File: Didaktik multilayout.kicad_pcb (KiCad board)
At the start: 2 copper layers, 212.7 x 79.4 mm, 121 parts, among them J1 Conn_01x04_MountingPin, J2 AVR-ISP-6, SW1 SW_Push_45deg, SW10 SW_Push_45deg, SW11 SW_Push_45deg, SW12 SW_Push_45deg, SW13 SW_Push_45deg, SW14 SW_Push_45deg, SW15 SW_Push_45deg, SW16 SW_Push_45deg, SW17 SW_Push_45deg, SW18 SW_Push_45deg, SW19 SW_Push_45deg, SW2 SW_Push_45deg, SW20 SW_Push_45deg, SW21 SW_Push_45deg, SW22 SW_Push_45deg, SW23 SW_Push_45deg, SW24 SW_Push_45deg, SW25 SW_Push_45deg, SW26 SW_Push_45deg, SW27 SW_Push_45deg, SW28 SW_Push_45deg, SW29 SW_Push_45deg, SW3 SW_Push_45deg, SW30 SW_Push_45deg, SW31 SW_Push_45deg, SW31a1 SW_Push_45deg, SW32 SW_Push_45deg, SW32a1 SW_Push_45deg, SW33 SW_Push_45deg, SW33a1 SW_Push_45deg, SW34 SW_Push_45deg, SW34a1 SW_Push_45deg, SW34b1 SW_Push_45deg, SW35 SW_Push_45deg, SW35a1 SW_Push_45deg, SW35b1 SW_Push_45deg, SW35c1 SW_Push_45deg, SW36 SW_Push_45deg, SW36a1 SW_Push_45deg, SW36b1 SW_Push_45deg, SW36c1 SW_Push_45deg, SW37 SW_Push_45deg, SW37a1 SW_Push_45deg, SW37b1 SW_Push_45deg, SW38 SW_Push_45deg, SW38a1 SW_Push_45deg, SW39 SW_Push_45deg, SW39a1 SW_Push_45deg, SW4 SW_Push_45deg, SW40 SW_Push_45deg, SW40a1 SW_Push_45deg, SW5 SW_Push_45deg, SW6 SW_Push_45deg, SW7 SW_Push_45deg, SW8 SW_Push_45deg, SW9 SW_Push_45deg, U1 ATmega32U4-M, Y1 Crystal_GND24_Small

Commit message: routing multipcb
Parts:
- moved D33 19.0 mm to (203.2, 106.4)
- moved D37 11.1 mm to (214.3, 104.8)
- moved D20 9.53 mm to (136.5, 104.8)
- moved D29 9.53 mm to (174.6, 104.8)
- moved D12 9.52 mm to (98.4, 104.8)
- moved D24 9.52 mm to (155.6, 106.4)
- moved D16 6.35 mm to (114.3, 106.4)
- moved D32 6.35 mm to (200.0, 87.3)
- moved D41 4.76 mm to (231.8, 106.4)
- moved D7 4.76 mm to (84.1, 87.3)
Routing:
- net COL2: track 307.6 -> 372.0 mm
- net +5V: track 323.7 -> 284.8 mm
- net MISO: track 37.2 -> 0.00 mm, vias 2 -> 0
- net MOSI: track 34.8 -> 0.00 mm, vias 2 -> 0
- net SCK: track 31.5 -> 0.00 mm, vias 2 -> 0
- net ROW4: track 374.4 -> 403.8 mm
- net ROW5: track 351.7 -> 379.5 mm
- net Net-(D33-Pad2): track 18.3 -> 45.4 mm
- net COL4: track 395.4 -> 419.1 mm
- net Net-(D12-Pad2): track 14.7 -> 37.9 mm, vias 0 -> 2
- net Net-(D8-Pad2): track 18.5 -> 40.9 mm
- net COL3: track 354.0 -> 375.3 mm
- net Net-(D24-Pad2): track 18.3 -> 38.3 mm
- net Net-(D20-Pad2): track 14.7 -> 34.2 mm, vias 0 -> 2
- net Net-(SW34b1-Pad2): track 18.3 -> 34.6 mm
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
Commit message: set up multilayout
need to check if all switches are really routed
maybe get rid of 2U
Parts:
- moved J2 168.8 mm to (69.8, 81.2)
- moved G*** 0.76 mm to (136.5, 85.0)
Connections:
- D12 pad 2: Net-(D12-Pad2) -> COL0
- D16 pad 2: Net-(SW34b1-Pad2) -> COL1
- D20 pad 2: Net-(D20-Pad2) -> COL1
- D24 pad 2: Net-(D24-Pad2) -> COL1
- D33 pad 2: Net-(D33-Pad2) -> COL3
- D37 pad 2: Net-(D37-Pad2) -> COL4
- D41 pad 2: Net-(D41-Pad2) -> COL4
- SW15 pad 1: COL2 -> COL1
- SW16 pad 1: COL2 -> COL1
- SW25 pad 1: COL2 -> COL1
- SW26 pad 1: COL2 -> COL1
- SW34 pad 2: Net-(SW34b1-Pad2) -> COL1
- SW34a1 pad 2: Net-(SW34b1-Pad2) -> COL1
- SW34b1 pad 2: Net-(SW34b1-Pad2) -> COL1
- SW35 pad : (no net) -> COL1
- SW35 pad 1: COL2 -> COL1
- SW35 pad 2: Net-(D20-Pad2) -> COL1
- SW35a1 pad : (no net) -> COL1
- SW35a1 pad 1: COL2 -> COL1
- SW35a1 pad 2: Net-(D20-Pad2) -> COL1
- SW35b1 pad : (no net) -> COL1
- SW35b1 pad 1: COL2 -> COL1
- SW35b1 pad 2: Net-(D20-Pad2) -> COL1
- SW35c1 pad 1: COL2 -> COL1
- SW35c1 pad 2: Net-(D20-Pad2) -> COL1
- SW36 pad : (no net) -> COL1
- SW36 pad 1: COL2 -> COL1
- SW36 pad 2: Net-(D24-Pad2) -> COL1
- SW36a1 pad : (no net) -> COL1
- SW36a1 pad 1: COL2 -> COL1
- SW36a1 pad 2: Net-(D24-Pad2) -> COL1
- SW36b1 pad : (no net) -> COL1
- SW36b1 pad 1: COL2 -> COL1
- SW36b1 pad 2: Net-(D24-Pad2) -> COL1
- SW36c1 pad 1: COL2 -> COL1
- SW36c1 pad 2: Net-(D20-Pad2) -> COL1
- SW37b1 pad : (no net) -> COL1
- SW5 pad 1: COL2 -> COL1
- SW6 pad 1: COL2 -> COL1
- U1 pad 20: unconnected-(U1-Pad20) -> SCK
- U1 pad 21: ROW5 -> MISO
- U1 pad 22: ROW4 -> MOSI
- U1 pad 26: MOSI -> unconnected-(U1-Pad26)
- U1 pad 27: SCK -> ROW7
- U1 pad 28: MISO -> ROW6
- U1 pad 29: ROW7 -> ROW5
- U1 pad 30: ROW6 -> ROW4
- U1 pad 37: COL2 -> COL1
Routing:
- net COL1: track 279.3 -> 793.9 mm, vias 1 -> 8
- net COL2: track 372.0 -> 0.00 mm, vias 1 -> 0
- net COL3: track 375.3 -> 453.7 mm, vias 1 -> 3
- net COL4: track 419.1 -> 494.2 mm, vias 1 -> 5
- net Net-(D33-Pad2): track 45.4 -> 0.00 mm, vias 2 -> 0
- net MOSI: track 0.00 -> 39.2 mm, vias 0 -> 2
- net Net-(D24-Pad2): track 38.3 -> 0.00 mm, vias 2 -> 0
- net SCK: track 0.00 -> 38.2 mm, vias 0 -> 2
- net Net-(D12-Pad2): track 37.9 -> 0.00 mm, vias 2 -> 0
- net COL0: track 246.2 -> 282.5 mm, vias 1 -> 3
- net Net-(SW34b1-Pad2): track 34.6 -> 0.00 mm, vias 2 -> 0
- net Net-(D20-Pad2): track 34.2 -> 0.00 mm, vias 2 -> 0
- net MISO: track 0.00 -> 34.1 mm, vias 0 -> 2
- net +5V: track 284.8 -> 318.9 mm, vias 5 -> 7
- net Net-(D41-Pad2): track 31.6 -> 0.00 mm, vias 2 -> 0
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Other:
- board text added: "1.5U"
- board text added: "2U"
- board text added: "3U"
- board text added: "6U"
- board text added: "7U"
- board text added: "check rewiring and pcb border"
- board text removed: "reset set up"
- board text removed: "rewiring everything"

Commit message: changes
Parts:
- added SW1: SW_Push_45deg, Keebio-Parts:MX-Alps-Choc-1U-NoLED, F.Cu at (21.6, 40.3)
- added SW10: SW_Push_45deg, Keebio-Parts:MX-Alps-Choc-1U-NoLED, F.Cu at (103.9, 169.7)
- added SW11: SW_Push_45deg, Keebio-Parts:MX-Alps-Choc-1U-NoLED, F.Cu at (114.6, 210.1)
- added SW12: SW_Push_45deg, Keebio-Parts:MX-Alps-Choc-1U-NoLED, F.Cu at (144.3, 169.7)
- added SW13: SW_Push_45deg, Keebio-Parts:MX-Alps-Choc-1U-NoLED, F.Cu at (74.2, 230.3)
- added SW14: SW_Push_45deg, Keebio-Parts:MX-Alps-Choc-1U-NoLED, F.Cu at (103.9, 149.5)
- added SW15: SW_Push_45deg, Keebio-Parts:MX-Alps-Choc-1U-NoLED, F.Cu at (175.2, 230.3)
- added SW16: SW_Push_45deg, Keebio-Parts:MX-Alps-Choc-1U-NoLED, F.Cu at (164.5, 169.7)
- added SW17: SW_Push_45deg, Keebio-Parts:MX-Alps-Choc-1U-NoLED, F.Cu at (114.6, 189.9)
- added SW18: SW_Push_45deg, Keebio-Parts:MX-Alps-Choc-1U-NoLED, F.Cu at (175.2, 189.9)
- added SW19: SW_Push_45deg, Keebio-Parts:MX-Alps-Choc-1U-NoLED, F.Cu at (124.1, 149.5)
- added SW2: SW_Push_45deg, Keebio-Parts:MX-Alps-Choc-1U-NoLED, F.Cu at (164.5, 149.5)
- added SW20: SW_Push_45deg, Keebio-Parts:MX-Alps-Choc-1U-NoLED, F.Cu at (175.2, 210.1)
- added SW21: SW_Push_45deg, Keebio-Parts:MX-Alps-Choc-1U-NoLED, F.Cu at (225.1, 149.5)
- added SW22: SW_Push_45deg, Keebio-Parts:MX-Alps-Choc-1U-NoLED, F.Cu at (134.8, 230.3)
- added SW23: SW_Push_45deg, Keebio-Parts:MX-Alps-Choc-1U-NoLED, F.Cu at (83.7, 169.7)
- added SW24: SW_Push_45deg, Keebio-Parts:MX-Alps-Choc-1U-NoLED, F.Cu at (184.7, 149.5)
- added SW25: SW_Push_45deg, Keebio-Parts:MX-Alps-Choc-1U-NoLED, F.Cu at (204.9, 149.5)
- added SW26: SW_Push_45deg, Keebio-Parts:MX-Alps-Choc-1U-NoLED, F.Cu at (134.8, 210.1)
- added SW27: SW_Push_45deg, Keebio-Parts:MX-Alps-Choc-1U-NoLED, F.Cu at (195.4, 189.9)
- added SW28: SW_Push_45deg, Keebio-Parts:MX-Alps-Choc-1U-NoLED, F.Cu at (74.2, 210.1)
- added SW29: SW_Push_45deg, Keebio-Parts:MX-Alps-Choc-1U-NoLED, F.Cu at (83.7, 149.5)
- added SW3: SW_Push_45deg, Keebio-Parts:MX-Alps-Choc-1U-NoLED, F.Cu at (94.4, 189.9)
- added SW30: SW_Push_45deg, Keebio-Parts:MX-Alps-Choc-1U-NoLED, F.Cu at (94.4, 230.3)
- added SW31: SW_Push_45deg, Keebio-Parts:MX-Alps-Choc-1.5U-NoLED, F.Cu at (58.7, 169.7)
- added SW32: SW_Push_45deg, Keebio-Parts:MX-Alps-Choc-1U-NoLED, F.Cu at (155.0, 189.9)
- added SW33: SW_Push_45deg, Keebio-Parts:MX-Alps-Choc-1U-NoLED, F.Cu at (54.0, 210.1)
- added SW34: SW_Push_45deg, Keebio-Parts:MX-Alps-Choc-1U-NoLED, F.Cu at (155.0, 230.3)
- added SW35: SW_Push_45deg, Keebio-Parts:MX-Alps-Choc-1U-NoLED, F.Cu at (26.7, 175.6)
- added SW36: SW_Push_45deg, Keebio-Parts:MX-Alps-Choc-1U-NoLED, F.Cu at (114.6, 230.3)
- added SW37: SW_Push_45deg, Keebio-Parts:MX-Alps-Choc-1U-NoLED, F.Cu at (74.2, 189.9)
- added SW38: SW_Push_45deg, Keebio-Parts:MX-Alps-Choc-1U-NoLED, F.Cu at (144.3, 149.5)
- added SW39: SW_Push_45deg, Keebio-Parts:MX-Alps-Choc-1U-NoLED, F.Cu at (155.0, 210.1)
- added SW4: SW_Push_45deg, Keebio-Parts:MX-Alps-Choc-1U-NoLED, F.Cu at (184.7, 169.7)
- added SW40: SW_Push_45deg, Keebio-Parts:MX-Alps-Choc-1.5U-NoLED, F.Cu at (58.7, 149.5)
- added SW5: SW_Push_45deg, Keebio-Parts:MX-Alps-Choc-1U-NoLED, F.Cu at (134.8, 189.9)
- added SW6: SW_Push_45deg, Keebio-Parts:MX-Alps-Choc-1U-NoLED, F.Cu at (94.4, 210.1)
- added SW7: SW_Push_45deg, Keebio-Parts:MX-Alps-Choc-1U-NoLED, F.Cu at (204.9, 169.7)
- added SW8: SW_Push_45deg, Keebio-Parts:MX-Alps-Choc-1U-NoLED, F.Cu at (225.1, 169.7)
- added SW9: SW_Push_45deg, Keebio-Parts:MX-Alps-Choc-1U-NoLED, F.Cu at (124.1, 169.7)
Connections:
- D12 pad 2: COL0 -> Net-(D12-Pad2)
- D16 pad 2: COL1 -> Net-(D16-Pad2)
- D20 pad 2: COL1 -> Net-(D20-Pad2)
- D24 pad 2: COL1 -> Net-(D24-Pad2)
- D33 pad 2: COL3 -> Net-(D33-Pad2)
- D37 pad 2: COL4 -> Net-(D37-Pad2)
- D41 pad 2: COL4 -> Net-(D41-Pad2)
- SW34a1 pad 2: COL1 -> Net-(D16-Pad2)
- SW34b1 pad 2: COL1 -> Net-(D16-Pad2)
- SW35a1 pad : COL1 -> (no net)
- SW35a1 pad 1: COL1 -> COL2
- SW35a1 pad 2: COL1 -> Net-(D20-Pad2)
- SW35b1 pad : COL1 -> (no net)
- SW35b1 pad 1: COL1 -> COL2
- SW35b1 pad 2: COL1 -> Net-(D20-Pad2)
- SW35c1 pad 1: COL1 -> COL2
- SW35c1 pad 2: COL1 -> Net-(D20-Pad2)
- SW36a1 pad : COL1 -> (no net)
- SW36a1 pad 1: COL1 -> COL2
- SW36a1 pad 2: COL1 -> Net-(D24-Pad2)
- SW36b1 pad : COL1 -> (no net)
- SW36b1 pad 1: COL1 -> COL2
- SW36b1 pad 2: COL1 -> Net-(D24-Pad2)
- SW36c1 pad 1: COL1 -> COL2
- SW36c1 pad 2: COL1 -> Net-(D20-Pad2)
- SW37b1 pad : COL1 -> (no net)
- U1 pad 37: COL1 -> COL2
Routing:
- net GND: track 53.5 -> 61.6 mm, vias 17 -> 18
- net (no net): vias 0 -> 1
- added copper zone on B.Cu, net (none)
- added copper zone on F.Cu, net (none)
- removed copper zone on B.Cu, net GND
- removed copper zone on F.Cu, net GND

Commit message: cleaning up the schematics / pcb for multi
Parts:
- removed the SW1 at (41.3, 41.3)
- removed the SW10 at (103.9, 169.7)
- removed the SW11 at (114.6, 210.1)
- removed the SW12 at (144.3, 169.7)
- removed the SW13 at (74.2, 230.3)
- removed the SW14 at (108.0, 60.3)
- removed the SW15 at (127.0, 60.3)
- removed the SW16 at (164.5, 169.7)
- removed the SW17 at (114.6, 189.9)
- removed the SW18 at (175.2, 189.9)
- removed the SW19 at (124.1, 149.5)
- removed the SW2 at (60.3, 41.3)
- removed the SW20 at (222.2, 60.3)
- removed the SW21 at (60.3, 79.4)
- removed the SW22 at (79.4, 79.4)
- removed the SW23 at (83.7, 169.7)
- removed the SW24 at (117.5, 79.4)
- removed the SW25 at (204.9, 149.5)
- removed the SW26 at (134.8, 210.1)
- removed the SW27 at (174.6, 79.4)
- removed the SW28 at (74.2, 210.1)
- removed the SW29 at (212.7, 79.4)
- removed the SW3 at (94.4, 189.9)
- removed the SW30 at (94.4, 230.3)
- removed the SW31 at (58.7, 169.7)
- removed the SW32 at (155.0, 189.9)
- removed the SW33 at (54.0, 210.1)
- removed the SW34 at (155.0, 230.3)
- removed the SW35 at (26.7, 175.6)
- removed the SW36 at (114.6, 230.3)
- removed the SW37 at (74.2, 189.9)
- removed the SW38 at (144.3, 149.5)
- removed the SW39 at (155.0, 210.1)
- removed the SW4 at (184.7, 169.7)
- removed the SW40 at (58.7, 149.5)
- removed the SW5 at (117.5, 41.3)
- removed the SW6 at (136.5, 41.3)
- removed the SW7 at (155.6, 41.3)
- removed the SW8 at (174.6, 41.3)
- removed the SW9 at (124.1, 169.7)
- moved SW21 179.1 mm to (60.3, 79.4)
- moved SW15 176.6 mm to (127.0, 60.3)
- moved SW6 173.9 mm to (136.4, 41.3)
- moved SW22 160.7 mm to (79.4, 79.4)
- moved SW20 157.0 mm to (222.2, 60.3)
- moved SW2 150.2 mm to (60.3, 41.3)
- moved SW5 149.6 mm to (117.5, 41.3)
- moved SW29 146.8 mm to (212.7, 79.4)
- moved SW8 138.0 mm to (174.6, 41.3)
- moved SW7 137.5 mm to (155.6, 41.3)
- moved SW27 112.4 mm to (174.6, 79.4)
- moved SW24 97.1 mm to (117.5, 79.4)
- moved SW14 89.2 mm to (108.0, 60.3)
- moved SW1 19.7 mm to (41.3, 41.3)
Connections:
- SW16 pad 1: COL1 -> COL2
- SW25 pad 1: COL1 -> COL2
- SW26 pad 1: COL1 -> COL2
- SW33 pad 1: COL1 -> (no net)
- SW33 pad 2: Net-(D12-Pad2) -> (no net)
- SW34 pad 2: COL1 -> Net-(D16-Pad2)
- SW35 pad : COL1 -> (no net)
- SW35 pad 1: COL1 -> COL2
- SW35 pad 2: COL1 -> Net-(D20-Pad2)
- SW36 pad : COL1 -> (no net)
- SW36 pad 1: COL1 -> COL2
- SW36 pad 2: COL1 -> Net-(D24-Pad2)
- SW9 pad 1: COL4 -> (no net)
- SW9 pad 2: Net-(D34-Pad2) -> (no net)
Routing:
- net COL2: track 0.00 -> 793.9 mm, vias 0 -> 8
- net COL1: track 793.9 -> 0.00 mm, vias 8 -> 0
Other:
- board text removed: "Didaktik 40"

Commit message: work on multi
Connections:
- SW33 pad 1: (no net) -> COL1
- SW33 pad 2: (no net) -> Net-(D12-Pad2)
- SW9 pad 1: (no net) -> COL4
- SW9 pad 2: (no net) -> Net-(D34-Pad2)
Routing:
- net (no net): track 0.00 -> 8.54 mm, vias 1 -> 3
- net GND: track 61.6 -> 53.4 mm, vias 18 -> 16

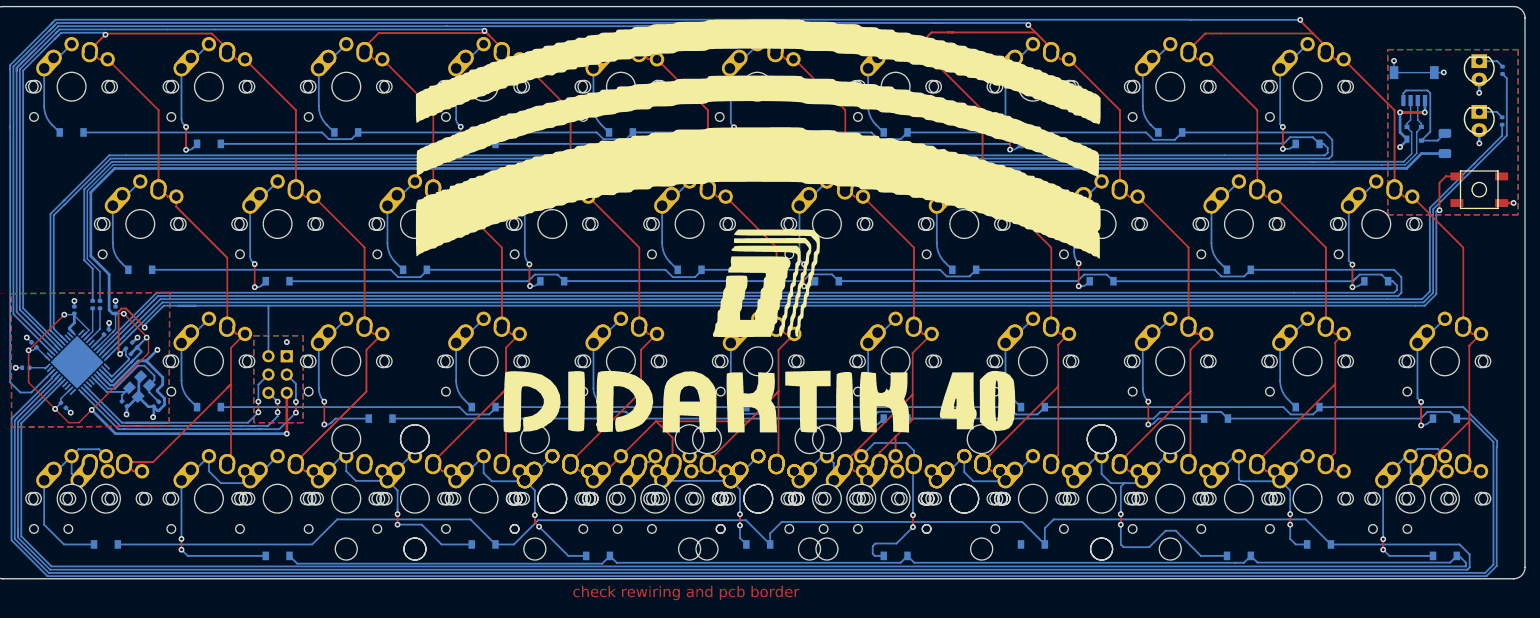
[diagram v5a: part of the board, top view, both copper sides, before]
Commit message: simplifying schematics, rerouting pcb
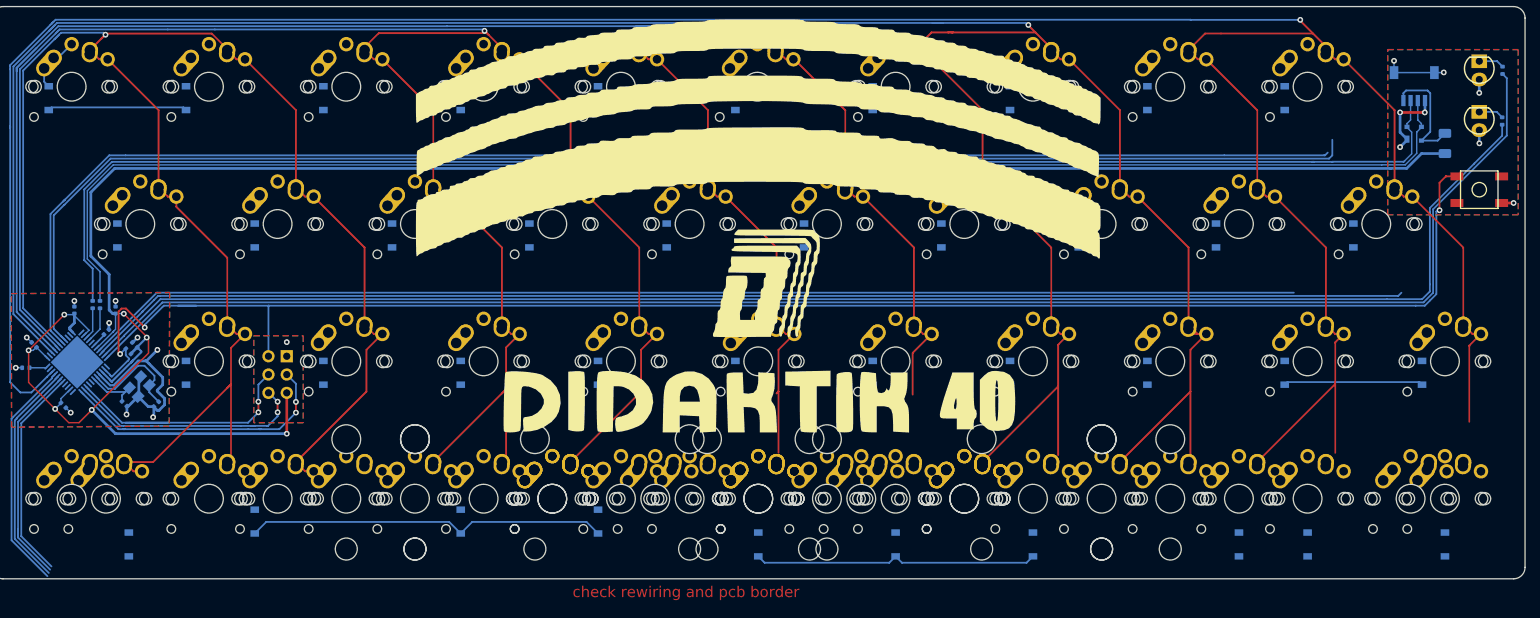
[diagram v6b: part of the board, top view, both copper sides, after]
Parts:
- moved D32 11.4 mm to (190.5, 81.0), turned to 90 degrees
- moved D7 10.2 mm to (76.2, 81.0), turned to 90 degrees
- moved D21 7.10 mm to (133.3, 42.9), turned to 90 degrees
- moved D22 7.10 mm to (142.9, 61.9), turned to 90 degrees
- moved D30 7.10 mm to (171.4, 42.9), turned to 90 degrees
- moved D31 7.10 mm to (181.0, 61.9), turned to 90 degrees
- moved D39 7.10 mm to (219.1, 61.9), turned to 90 degrees
- moved D5 7.10 mm to (57.1, 42.9), turned to 90 degrees
- moved D13 7.10 mm to (95.2, 42.9), turned to 90 degrees
- moved D14 7.10 mm to (104.8, 61.9), turned to 90 degrees
- moved D6 7.10 mm to (66.7, 61.9), turned to 90 degrees
- moved D40 7.10 mm to (228.6, 81.0), turned to 90 degrees
- moved D15 7.10 mm to (114.3, 81.0), turned to 90 degrees
- moved D38 7.10 mm to (209.6, 42.9), turned to 90 degrees
- moved D23 7.10 mm to (152.4, 81.0), turned to -90 degrees
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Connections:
- net Net-(C3-Pad2) renamed XTAL1
- net Net-(C4-Pad2) renamed XTAL2
- D10 pad 1: ROW2 -> ROW1
- D11 pad 1: ROW4 -> ROW2
- D12 pad 1: ROW6 -> ROW3
- D13 pad 1: ROW1 -> ROW0
- D14 pad 1: ROW3 -> ROW1
- D15 pad 1: ROW5 -> ROW2
- D16 pad 1: ROW7 -> ROW3
- D18 pad 1: ROW2 -> ROW1
- D19 pad 1: ROW4 -> ROW2
- D2 pad 1: ROW2 -> ROW1
- D20 pad 1: ROW6 -> ROW3
- D21 pad 1: ROW1 -> ROW0
- D22 pad 1: ROW3 -> ROW1
- D23 pad 1: ROW5 -> ROW2
- D24 pad 1: ROW7 -> ROW3
- D27 pad 1: ROW2 -> ROW1
- D28 pad 1: ROW4 -> ROW2
- D29 pad 1: ROW6 -> ROW3
- D3 pad 1: ROW4 -> ROW2
- D30 pad 1: ROW1 -> ROW0
- D31 pad 1: ROW3 -> ROW1
- D32 pad 1: ROW5 -> ROW2
- D33 pad 1: ROW7 -> ROW3
- D35 pad 1: ROW2 -> ROW1
- D36 pad 1: ROW4 -> ROW2
- D37 pad 1: ROW6 -> ROW3
- D38 pad 1: ROW1 -> ROW0
- D39 pad 1: ROW3 -> ROW1
- D4 pad 1: ROW6 -> ROW3
- D40 pad 1: ROW5 -> ROW2
- D41 pad 1: ROW7 -> ROW3
- D5 pad 1: ROW1 -> ROW0
- D6 pad 1: ROW3 -> ROW1
- D7 pad 1: ROW5 -> ROW2
- D8 pad 1: ROW7 -> ROW3
- SW10 pad 1: COL4 -> COL9
- SW12 pad 1: COL0 -> COL1
- SW13 pad 1: COL1 -> COL2
- SW14 pad 1: COL1 -> COL3
- SW15 pad 1: COL2 -> COL4
- SW16 pad 1: COL2 -> COL5
- SW17 pad 1: COL3 -> COL6
- SW18 pad 1: COL3 -> COL7
- SW19 pad 1: COL4 -> COL8
- SW2 pad 1: COL0 -> COL1
- SW20 pad 1: COL4 -> COL9
- SW22 pad 1: COL0 -> COL1
- SW23 pad 1: COL1 -> COL2
- SW24 pad 1: COL1 -> COL3
- SW25 pad 1: COL2 -> COL4
- SW26 pad 1: COL2 -> COL5
- SW27 pad 1: COL3 -> COL6
- SW28 pad 1: COL3 -> COL7
- SW29 pad 1: COL4 -> COL8
- SW3 pad 1: COL1 -> COL2
- SW30 pad 1: COL4 -> COL9
- SW31 pad 1: COL0 -> unconnected-(SW31-Pad1)
- SW32 pad 1: COL0 -> unconnected-(SW32-Pad1)
- SW32a1 pad 1: COL0 -> COL1
- SW33 pad 1: COL1 -> unconnected-(SW33-Pad1)
- SW33a1 pad 1: COL1 -> COL2
- SW34 pad 1: COL1 -> unconnected-(SW34-Pad1)
- SW34a1 pad 1: COL1 -> COL3
- SW34b1 pad 1: COL1 -> COL3
- SW35 pad 1: COL2 -> unconnected-(SW35-Pad1)
- SW35a1 pad 1: COL2 -> COL4
- SW35b1 pad 1: COL2 -> COL4
- SW35c1 pad 1: COL2 -> COL4
- SW36 pad 1: COL2 -> unconnected-(SW36-Pad1)
- SW36a1 pad 1: COL2 -> COL5
- SW36b1 pad 1: COL2 -> COL5
- SW36c1 pad 1: COL2 -> COL4
- SW37 pad 1: COL3 -> unconnected-(SW37-Pad1)
- SW37a1 pad 1: COL3 -> COL6
- SW37b1 pad 1: COL3 -> COL6
- SW38 pad 1: COL3 -> unconnected-(SW38-Pad1)
- SW38a1 pad 1: COL3 -> COL7
- SW39 pad 1: COL4 -> unconnected-(SW39-Pad1)
- SW39a1 pad 1: COL4 -> COL8
- SW4 pad 1: COL1 -> COL3
- SW40 pad 1: COL4 -> COL9
- SW40a1 pad 1: COL4 -> COL9
- SW5 pad 1: COL2 -> COL4
- SW6 pad 1: COL2 -> COL5
- SW7 pad 1: COL3 -> COL6
- SW8 pad 1: COL3 -> COL7
- SW9 pad 1: COL4 -> COL8
- U1 pad 12: unconnected-(U1-Pad12) -> COL9
- U1 pad 28: ROW6 -> COL6
- U1 pad 29: ROW5 -> COL7
- U1 pad 30: ROW4 -> COL8
- U1 pad 32: unconnected-(U1-Pad32) -> COL5
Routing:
- net COL2: track 793.9 -> 0.00 mm, vias 8 -> 0
- net COL3: track 453.7 -> 0.00 mm, vias 3 -> 0
- net ROW4: track 433.7 -> 0.00 mm
- net ROW6: track 432.0 -> 0.00 mm
- net COL6: track 0.00 -> 412.3 mm, vias 0 -> 1
- net ROW5: track 406.7 -> 0.00 mm
- net COL9: track 0.00 -> 403.6 mm, vias 0 -> 1
- net ROW7: track 393.3 -> 29.7 mm
- net COL0: track 282.5 -> 0.00 mm, vias 3 -> 0
- net COL1: track 0.00 -> 245.4 mm, vias 0 -> 1
- net ROW2: track 363.0 -> 203.3 mm
- net ROW1: track 357.1 -> 199.6 mm
- net ROW0: track 377.7 -> 220.3 mm
- net COL4: track 494.2 -> 591.5 mm, vias 5 -> 2
- net ROW3: track 341.2 -> 258.9 mm
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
